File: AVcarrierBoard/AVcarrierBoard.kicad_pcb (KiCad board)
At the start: 2 copper layers, 253.6 x 59 mm, 12 parts, among them J1 MainRecov, J2 RavenStaging, J3 DrogRecov, J4 Mech_Switch, J5 Mech_Switch, U1 EggfinderMini/FeatherGPS, U2 EggtimerQuark, U3 Blue_Raven, U4 WiFi Switch, U5 WiFi Switch

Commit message: ok ok
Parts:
- removed J2: RavenStaging, COTS_Boards:TE_282837-4
- added J6: 462070006, COTS_Boards:CON_462070006, F.Cu at (35.6, 78.0)
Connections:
- BT2 pad 2: GND -> GND2
- U3 pad 2: GND -> GND2
- U4 pad 2: GND -> GND2
- U4 pad 4: GND -> GND2
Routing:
- net DROG1: track 0.00 -> 204.7 mm, vias 0 -> 1
- net Raven3RD: track 0.00 -> 198.5 mm
- net Raven4TH: track 0.00 -> 191.6 mm, vias 0 -> 1
- net RavenMAIN: track 0.00 -> 191.4 mm
- net DROG2: track 0.00 -> 185.1 mm, vias 0 -> 1
- net WIFI_PWR_1S: track 0.00 -> 156.4 mm
- net RavenAPO: track 0.00 -> 75.5 mm
- net MAIN1: track 0.00 -> 70.4 mm
- net MAIN2: track 0.00 -> 70.3 mm
- added copper zone on In1.Cu, net +3V8
- added copper zone on F.Cu, net +7.5V
- added copper zone on B.Cu, net GND
- added copper zone on In2.Cu, net GND2
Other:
- copper layers 2 -> 4
- board text added: "Phoenix 1.0"

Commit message: edited
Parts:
- added H1: MountingHole, MountingHole:MountingHole_3.2mm_M3_ISO14580, F.Cu at (28.4, 70.7)
- added H2: MountingHole, MountingHole:MountingHole_3.2mm_M3_ISO14580, F.Cu at (269.6, 118.3)
- added H3: MountingHole, MountingHole:MountingHole_3.2mm_M3_ISO14580, F.Cu at (29.0, 119.4)
- added H4: MountingHole, MountingHole:MountingHole_3.2mm_M3_ISO14580, F.Cu at (269.8, 72.1)
- moved U1 9.18 mm to (59.3, 93.6)
- moved J6 8.00 mm to (43.6, 77.7)
- moved J1 2.45 mm to (29.5, 96.7)
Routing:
- net +3V8: track 0.00 -> 179.1 mm, vias 0 -> 1
- net GND: track 0.00 -> 147.9 mm, vias 0 -> 1
- net WIFI_PWR_1S: track 156.4 -> 303.6 mm
- net WIFI_PWR_2S: track 0.00 -> 132.4 mm
- net Raven4TH: track 191.6 -> 263.0 mm
- net GND2: track 0.00 -> 54.7 mm, vias 0 -> 1
- net +7.5V: track 0.00 -> 47.0 mm, vias 0 -> 1
- net COTSWIFI+: track 0.00 -> 46.5 mm
- net SRADWIFI+: track 0.00 -> 28.4 mm
- net DROG1: track 204.7 -> 184.2 mm
- net Raven3RD: track 198.5 -> 186.8 mm
- net RavenMAIN: track 191.4 -> 187.6 mm
- net MAIN2: track 70.3 -> 71.1 mm
- net MAIN1: track 70.4 -> 71.1 mm

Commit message: Added additional igniter switch, replaced quark with quantum, and updated PCB
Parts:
- removed the U5 at (117.1, 121.6)
- added J6: Mech_Switch, Connector_PinHeader_2.54mm:PinHeader_1x02_P2.54mm_Vertical, F.Cu at (83.8, 57.8)
- H1, H2, H3, H4: value MountingHole -> M3
- J5: renamed from J6; value 462070006 -> Staging
- U3: renamed from U2; value EggtimerQuark -> EggtimerQuantum; footprint COTS_Boards:EggtimerQuark -> COTS_Boards:EggtimerQuantum
- moved U3 63.2 mm to (105.5, 120.9), turned to 180 degrees
- renumbered J5 to J1, J4 to J2, J1 to J3, J3 to J4, U4 to U2, U1 to U4, U3 to U5
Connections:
- J5 pad 3: Raven3RD -> RavenMotIgnition
- J5 pad 5: Raven3RD -> RavenMotIgnition
- U3 pad 5: WIFI_PWR_2S -> SRADWIFI+
- U4 pad 1: WIFI_PWR_2S -> SRADWIFI+

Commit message: Updated PCB, made new nets and vias according to last change. Did not fill power layers yet.
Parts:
- moved J6 85.1 mm to (160.1, 95.5), turned to -90 degrees
- moved U3 65.9 mm to (44.4, 96.4), turned to 0 degrees
- moved J2 40.3 mm to (149.5, 101.4)
- moved U2 3.81 mm to (121.3, 69.1)
- moved J1 3.12 mm to (145.9, 93.5)
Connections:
- net SRADWIFI+ renamed PWR_2S
- BT1 pad 1: +7.5V -> RavenMotIgnition
- J1 pad 2: +7.5V -> RavenMotIgnition
- J4 pad 4: WIFI_PWR_1S -> RavenMotIgnition
- U5 pad 1: WIFI_PWR_1S -> RavenMotIgnition
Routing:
- net RavenMotIgnition: track 0.00 -> 367.9 mm, vias 0 -> 2
- net WIFI_PWR_1S: track 303.6 -> 115.4 mm
- net WIFI_PWR_2S: track 132.4 -> 0.00 mm
- net Raven3RD: track 186.8 -> 61.9 mm
- net GND: track 147.9 -> 221.6 mm
- net +7.5V: track 47.0 -> 0.00 mm, vias 1 -> 0
- net PWR_2S: track 28.4 -> 58.7 mm
- net COTSWIFI+: track 46.5 -> 73.5 mm
- net MAIN1: track 71.1 -> 93.9 mm
- net DROG2: track 185.1 -> 163.8 mm, vias 1 -> 0
- net MAIN2: track 71.1 -> 91.8 mm
- net DROG1: track 184.2 -> 184.3 mm, vias 1 -> 0

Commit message: Updated PCB further to avoid any DRC errors and missed connections
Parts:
- moved J1 4.90 mm to (144.5, 88.8), turned to 90 degrees
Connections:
- BT1 pad 1: RavenMotIgnition -> +7.5V
- J1 pad 2: RavenMotIgnition -> +7.5V
- J4 pad 4: RavenMotIgnition -> WIFI_PWR_1S
- U5 pad 1: RavenMotIgnition -> WIFI_PWR_1S
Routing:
- net RavenMotIgnition: track 367.9 -> 132.6 mm, vias 2 -> 1
- net WIFI_PWR_1S: track 115.4 -> 228.8 mm
- net GND: track 221.6 -> 118.4 mm
- net PWR_2S: track 58.7 -> 0.00 mm
- net +3V8: track 179.1 -> 121.1 mm
- net +7.5V: track 0.00 -> 39.0 mm, vias 0 -> 1
- net COTSWIFI+: track 73.5 -> 43.0 mm
- net DROG1: track 184.3 -> 177.6 mm
- net GND2: track 54.7 -> 50.9 mm
- added copper zone on F.Cu, net PWR_2S
- added copper zone on In1.Cu, net WIFI_PWR_1S
- removed copper zone on In1.Cu, net +3V8
- removed copper zone on F.Cu, net +7.5V

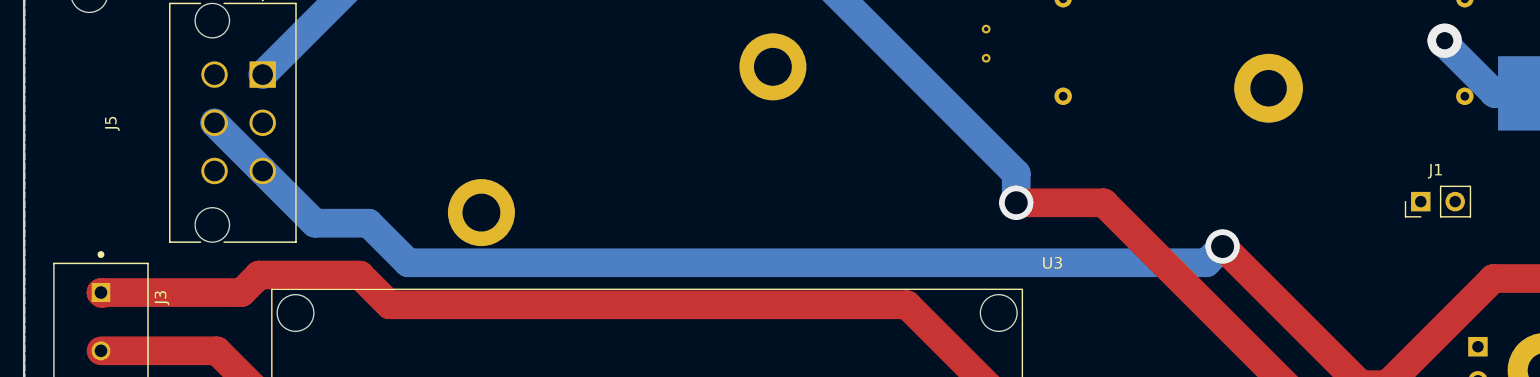
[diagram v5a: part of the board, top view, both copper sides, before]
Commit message: More PCB changes according to Ethan's review
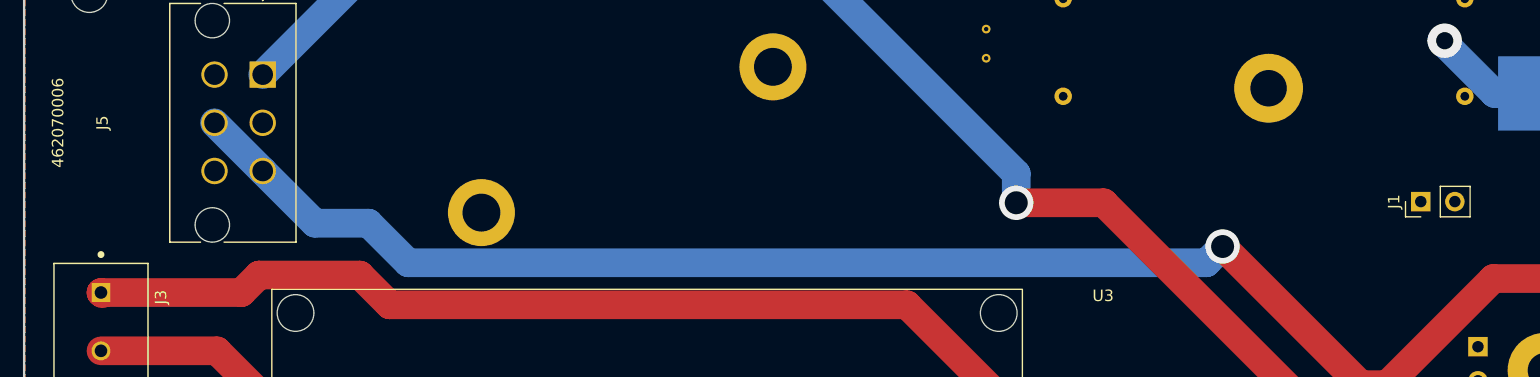
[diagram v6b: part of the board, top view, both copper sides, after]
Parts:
- J1, J2: footprint Connector_PinHeader_2.54mm:PinHeader_1x02_P2.54mm_Vertical -> Connector_PinHeader_2.54mm:PinHeader_1x02_P2.97mm_Vertical
- J3: footprint COTS_Boards:TE_282837-4 -> COTS_Boards:TE_282837-4-2
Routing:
- net WIFI_PWR_1S: track 228.8 -> 0.49 mm
- net GND: track 118.4 -> 12.5 mm
- net Raven4TH: track 263.0 -> 186.3 mm
- net GND2: track 50.9 -> 10.9 mm
